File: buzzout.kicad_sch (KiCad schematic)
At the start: 5 parts, among them J4 Conn_01x02_Pin, Q2 IRLML6402, U7 TC4428xOA

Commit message: sch, pcb: update pn fields
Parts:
- J4: Part Number (none) -> 1053091103
- JP4: Part Number (none) -> M20-9990246
- Q2: Part Number (none) -> IRLML6402TRPBF
- U7: Part Number (none) -> TC4428EOA713
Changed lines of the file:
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@@
+			)
+		)
+		(property "Part Number" "M20-9990246"
+			(at 144.78 92.71 0)
+			(effects
+				(font
+					(size 1.27 1.27)
+				)
+				(hide yes)
 			)
 		)
@@
 			)
 		)
+		(property "Part Number" "1053091103"
+			(at 153.67 109.22 0)
+			(effects
+				(font
+					(size 1.27 1.27)
+				)
+				(hide yes)
+			)
+		)
 		(pin "2"
 		)
@@
 			)
 		)
+		(property "Part Number" "TC4428EOA713"
+			(at 97.79 111.76 0)
+			(effects
+				(font
+					(size 1.27 1.27)
+				)
+				(hide yes)
+			)
+		)
 		(pin "1"
 		)
@@
 			(at 119.38 109.22 0)
 			(effects
+				(font
+					(size 1.27 1.27)
+				)
+				(hide yes)
+			)
+		)
+		(property "Part Number" "IRLML6402TRPBF"
+			(at 119.38 109.22 0)
+			(effects

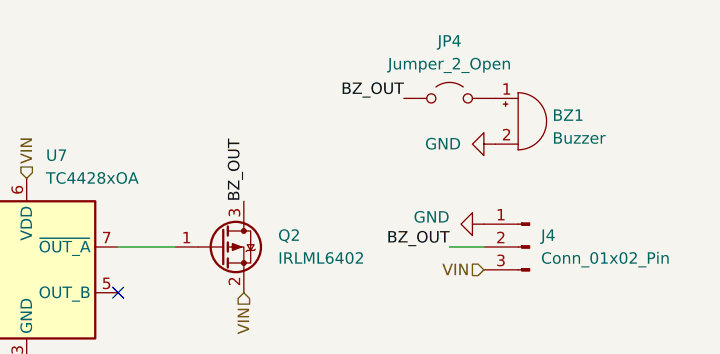
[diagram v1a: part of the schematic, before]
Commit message: buzzout, pcb: use dip switch for buzzer enable, pcb: servo output pin labels
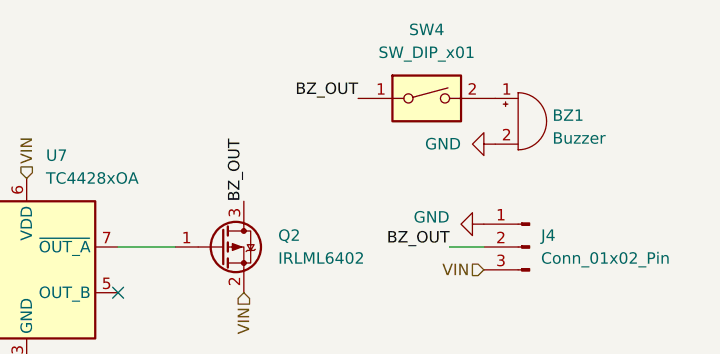
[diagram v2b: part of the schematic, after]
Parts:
- removed JP4: Jumper_2_Open, Connector_PinHeader_2.00mm:PinHeader_1x02_P2.00mm_Vertical, symbol Jumper:Jumper_2_Open
- added SW4: SW_DIP_x01, Button_Switch_SMD:SW_DIP_SPSTx01_Slide_Copal_CHS-01A_W5.08mm_P1.27mm_JPin, symbol Switch:SW_DIP_x01
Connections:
- net BZ_OUT: now also SW4.1
- net at BZ1.1 (+): now also SW4.2
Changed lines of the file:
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@@
 	)
 	(label "BZ_OUT"
-		(at 139.7 92.71 180)
+		(at 134.62 92.71 180)
 		(effects
 			(font
@@
 	)
 	(symbol
-		(lib_id "Jumper:Jumper_2_Open")
-		(at 144.78 92.71 0)
-		(unit 1)
-		(exclude_from_sim no)
-		(in_bom yes)
-		(on_board yes)
-		(dnp no)
-		(fields_autoplaced yes)
-		(property "Reference" "JP4"
-			(at 144.78 86.36 0)
-			(effects
-				(font
-					(size 1.27 1.27)
-				)
-			)
-		)
-		(property "Value" "Jumper_2_Open"
-			(at 144.78 88.9 0)
-			(effects
-				(font
-					(size 1.27 1.27)
-				)
-			)
-		)
-		(property "Footprint" "Connector_PinHeader_2.00mm:PinHeader_1x02_P2.00mm_Vertical"
-			(at 144.78 92.71 0)
-			(effects
-				(font
-					(size 1.27 1.27)
-				)
-				(hide yes)
-			)
-		)
-		(property "Datasheet" "~"
-			(at 144.78 92.71 0)
-			(effects
-				(font
-					(size 1.27 1.27)
-				)
-				(hide yes)
-			)
-		)
-		(property "Description" "Jumper, 2-pole, open"
-			(at 144.78 92.71 0)
-			(effects
-				(font
-					(size 1.27 1.27)
-				)
-				(hide yes)
-			)
-		)
-		(property "Part Number" "M20-9990246"
-			(at 144.78 92.71 0)
-			(effects
-				(font
-					(size 1.27 1.27)
-				)
-				(hide yes)
-			)
-		)
-		(pin "2"
-		)
-		(pin "1"
-		)
-		(instances
-			(project ""
-				(path "/362ca48c-0b77-4943-b8b3-fc15ab97f30d/441e8b1c-2de5-43eb-9608-83e9eae90220"
-					(reference "JP4")
-					(unit 1)
-				)
-			)
-		)
-	)
-	(symbol
 		(lib_id "power:GND")
 		(at 87.63 114.3 270)
@@
 					(unit 1)
 				)
+			)
+		)
+	)
+	(symbol
+		(lib_id "Switch:SW_DIP_x01")
+		(at 142.24 92.71 0)
+		(unit 1)
+		(exclude_from_sim no)
+		(in_bom yes)
+		(on_board yes)
+		(dnp no)
+		(fields_autoplaced yes)
+		(property "Reference" "SW4"
+			(at 142.24 85.09 0)
+			(effects
+				(font
+					(size 1.27 1.27)
+				)
+			)
+		)
+		(property "Value" "SW_DIP_x01"
+			(at 142.24 87.63 0)
+			(effects
+				(font
+					(size 1.27 1.27)
+				)
+			)
+		)
+		(property "Footprint" "Button_Switch_SMD:SW_DIP_SPSTx01_Slide_Copal_CHS-01A_W5.08mm_P1.27mm_JPin"
+			(at 142.24 92.71 0)
+			(effects
+				(font
+					(size 1.27 1.27)
+				)
+				(hide yes)
+			)
+		)
+		(property "Datasheet" "~"
+			(at 142.24 92.71 0)
+			(effects
+				(font
+					(size 1.27 1.27)
+				)
+				(hide yes)
+			)
+		)
+		(property "Description" "1x DIP Switch, Single Pole Single Throw (SPST) switch, small symbol"
+			(at 142.24 92.71 0)
+			(effects
+				(font
+					(size 1.27 1.27)
+				)
+				(hide yes)
+			)
+		)
+		(property "Part Number" "CHS-01A"
+			(at 142.24 92.71 0)
+			(effects
+				(font
+					(size 1.27 1.27)
+				)
+				(hide yes)
+			)
+		)
+		(pin "1"
+		)
+		(pin "2"
+		)
+		(instances
+			(project "P2 Kevinbot Board"
+				(path "/362ca48c-0b77-4943-b8b3-fc15ab97f30d/441e8b1c-2de5-43eb-9608-83e9eae90220"
+					(reference "SW4")
+					(unit 1)
+				)

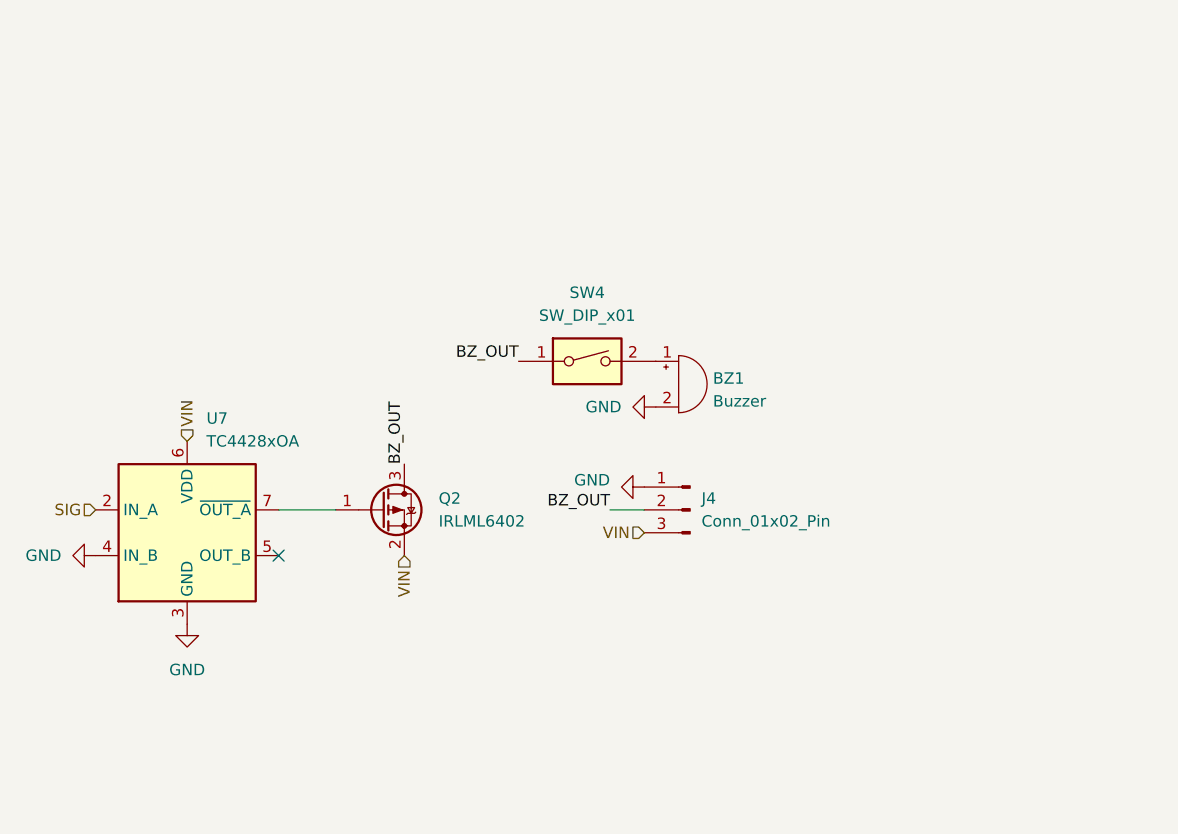
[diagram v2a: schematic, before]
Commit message: Update to latest footprints, cleanup
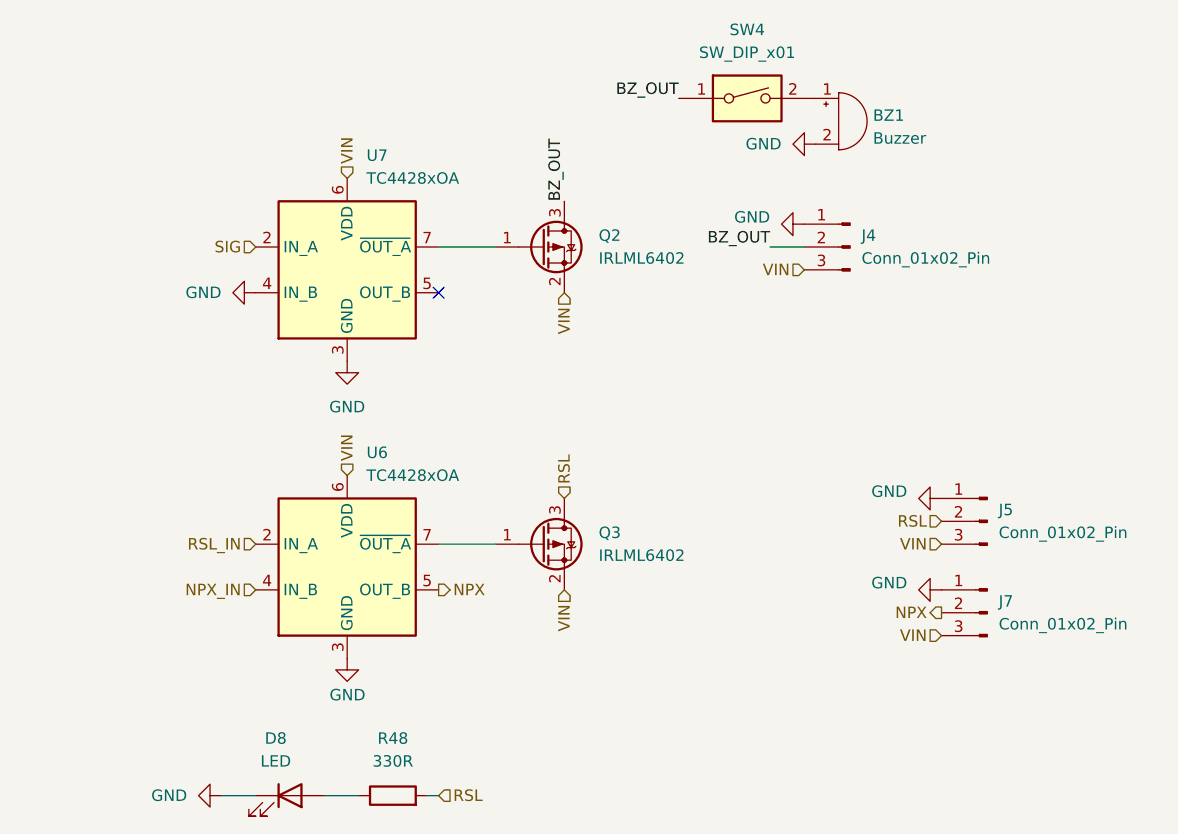
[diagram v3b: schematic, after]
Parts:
- added D8: LED, LED_SMD:LED_0603_1608Metric, symbol Device:LED
- added J5, J7: Conn_01x02_Pin, Connector_Molex:Molex_Nano-Fit_105309-xx03_1x03_P2.50mm_Vertical, symbol Connector:Conn_01x03_Pin
- added Q3: IRLML6402, Package_TO_SOT_SMD:SOT-23, symbol Transistor_FET:IRLML6402
- added R48: 330R, Resistor_SMD:R_0603_1608Metric, symbol Device:R
- added U6: TC4428xOA, Package_SO:SOIC-8_3.9x4.9mm_P1.27mm, symbol Driver_FET:TC4428xOA
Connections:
- net GND: now also D8.1 (K), J5.1 (Pin_1), J7.1 (Pin_1), U6.3 (GND)
- net VIN: now also J5.3 (Pin_3), J7.3 (Pin_3), Q3.2 (S), U6.6 (VDD)
- new net: Q3.1 (G), U6.7 (~{OUT_A})
- new net: D8.2 (A), R48.1
- new net NPX: J7.2 (Pin_2), U6.5 (OUT_B)
- new net NPX_IN: U6.4 (IN_B)
- new net RSL: J5.2 (Pin_2), Q3.3 (D), R48.2
- new net RSL_IN: U6.2 (IN_A)
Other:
- moved on the sheet: BZ1, J4, Q2, SW4, U7
